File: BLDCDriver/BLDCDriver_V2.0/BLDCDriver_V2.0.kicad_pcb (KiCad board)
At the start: 2 copper layers, 58 parts, among them J1 STLink, J2 Motor Out, J3 Conn_01x03, J4 PowerIN, Q1 SIZ254DT-T1-GE3, Q2 SIZ254DT-T1-GE3, Q3 SIZ254DT-T1-GE3, U1 (symbol "Device:C" (pin_numbe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, U3 MCP2562-E-SN

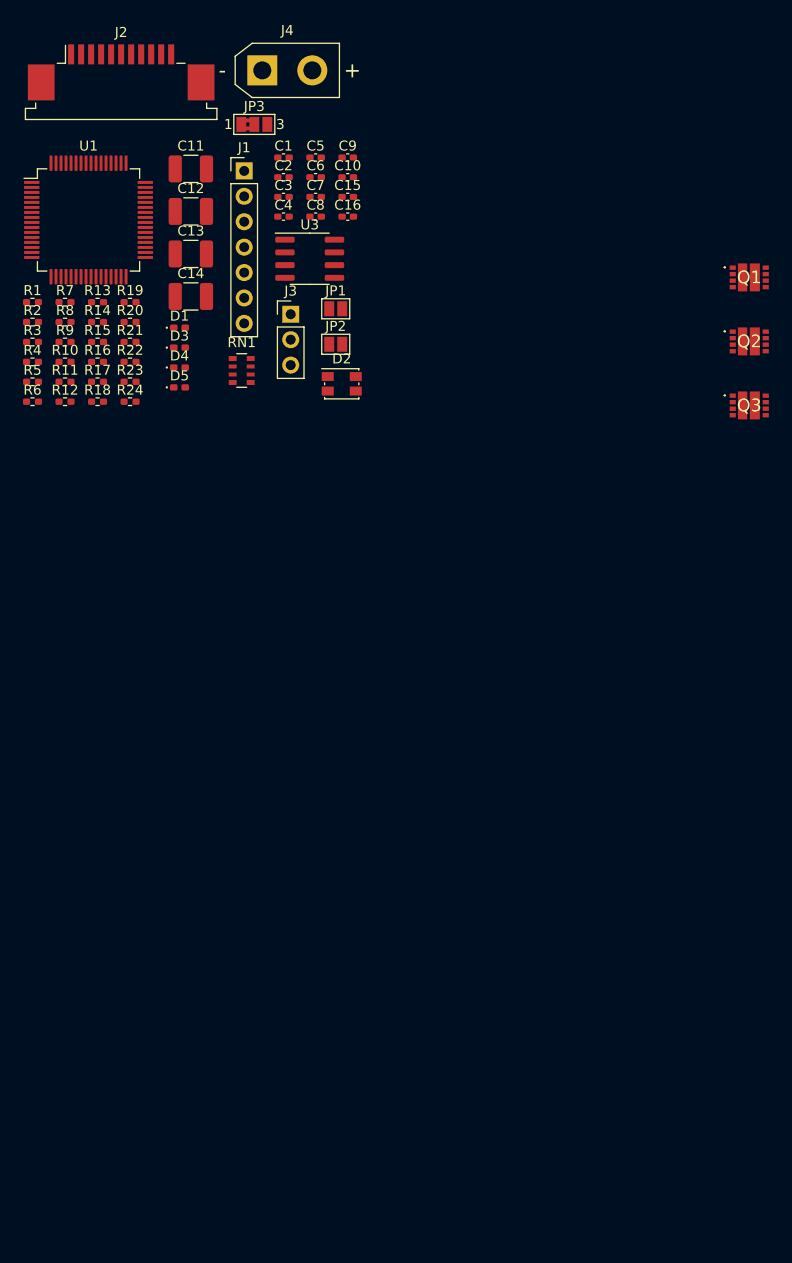
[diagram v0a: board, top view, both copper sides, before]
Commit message: :sparkles: V1.4 JLCPCBのPCBA検証用基板の設計DONE
# ==== Emojis ====
# ✨ :sparkles: Add new feature
# ✅  :white_check_mark: Update existing feature (not bug)
# ⚠️  :warning: Fix bug/error
# 🔥  :fire: Remove files or features
# ✏️ :pencil2: Fix typos
# 📝  :memo: Update documentation
# ♻️  :recycle: Dependencies update
# 🐧  :penguin: Improved the Linux
# 🍎  :apple: Improved the macOS
# 🔖 :bookmark: Add new library
# 🎉  :tada: Initial commit

# ==== Format ====
# :emoji: Subject
#
# Commit body...

# ==== Messages ====
# 新規(ファイル)機能追加: Add
# 機能修正、既存機能追加（バグではない): Update
# リファクタリング: Clean
# ファイル名変更:
# 削除など: Remove
# バグ修正: Fix
# バージョンアップ: Upgrade
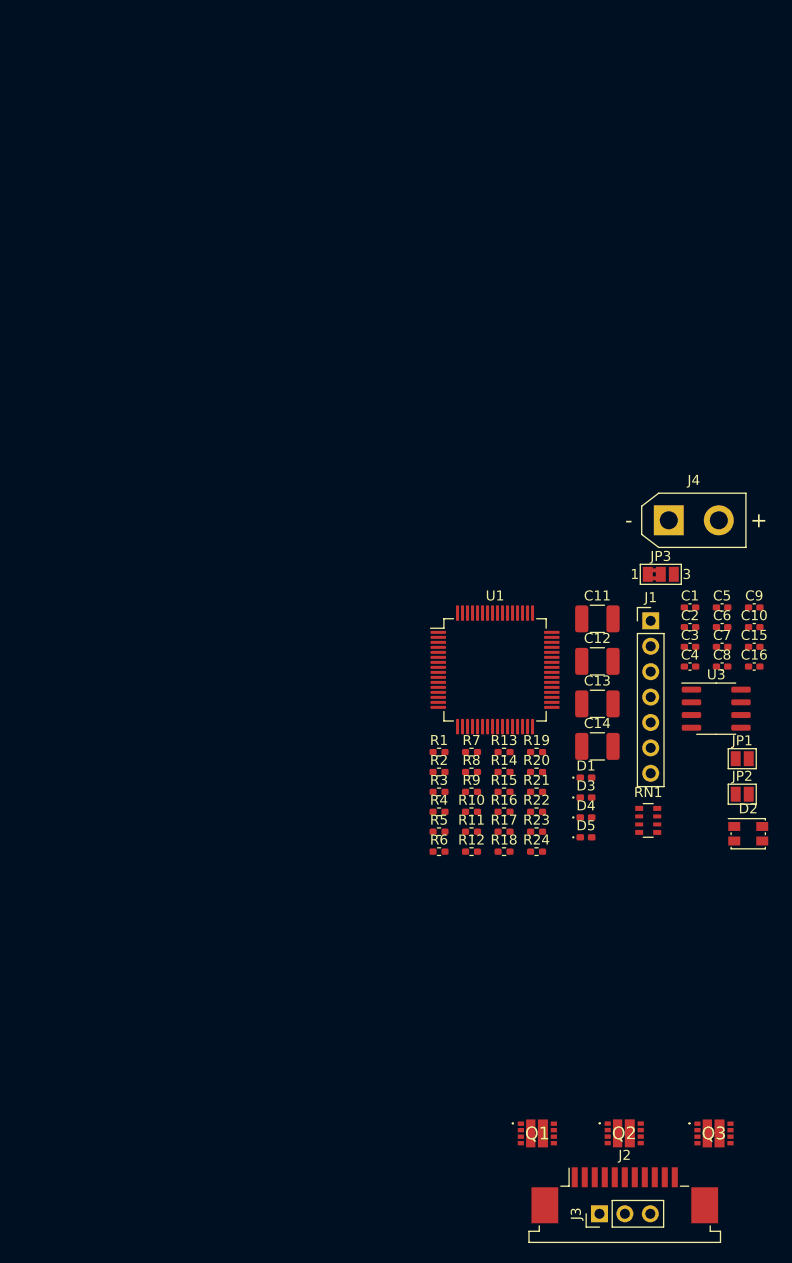
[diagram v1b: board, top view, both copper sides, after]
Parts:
- moved J2 123.0 mm to (60.3, 115.6)
- moved J3 95.1 mm to (57.8, 117.4), turned to 90 degrees
- moved Q1 88.2 mm to (51.6, 109.4)
- moved Q2 80.1 mm to (60.3, 109.4)
- moved Q3 72.9 mm to (69.2, 109.4)
- moved C10 60.6 mm to (73.3, 58.8)
- moved C15 60.6 mm to (73.3, 60.7)
- moved C16 60.6 mm to (73.3, 62.7)
- moved C2 60.6 mm to (66.8, 58.8)
- moved C3 60.6 mm to (66.8, 60.7)
- moved C4 60.6 mm to (66.8, 62.7)
- moved C6 60.6 mm to (70.1, 58.8)
- moved C7 60.6 mm to (70.1, 60.7)
- moved C8 60.6 mm to (70.1, 62.7)
- moved C9 60.6 mm to (73.3, 56.8)
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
